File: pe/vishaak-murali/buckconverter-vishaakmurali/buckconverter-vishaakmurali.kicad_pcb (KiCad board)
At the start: 2 copper layers, 42 x 28 mm, 7 parts, among them J1 VIN_IN, J2 VOUT_5V, U1 AP63205WU

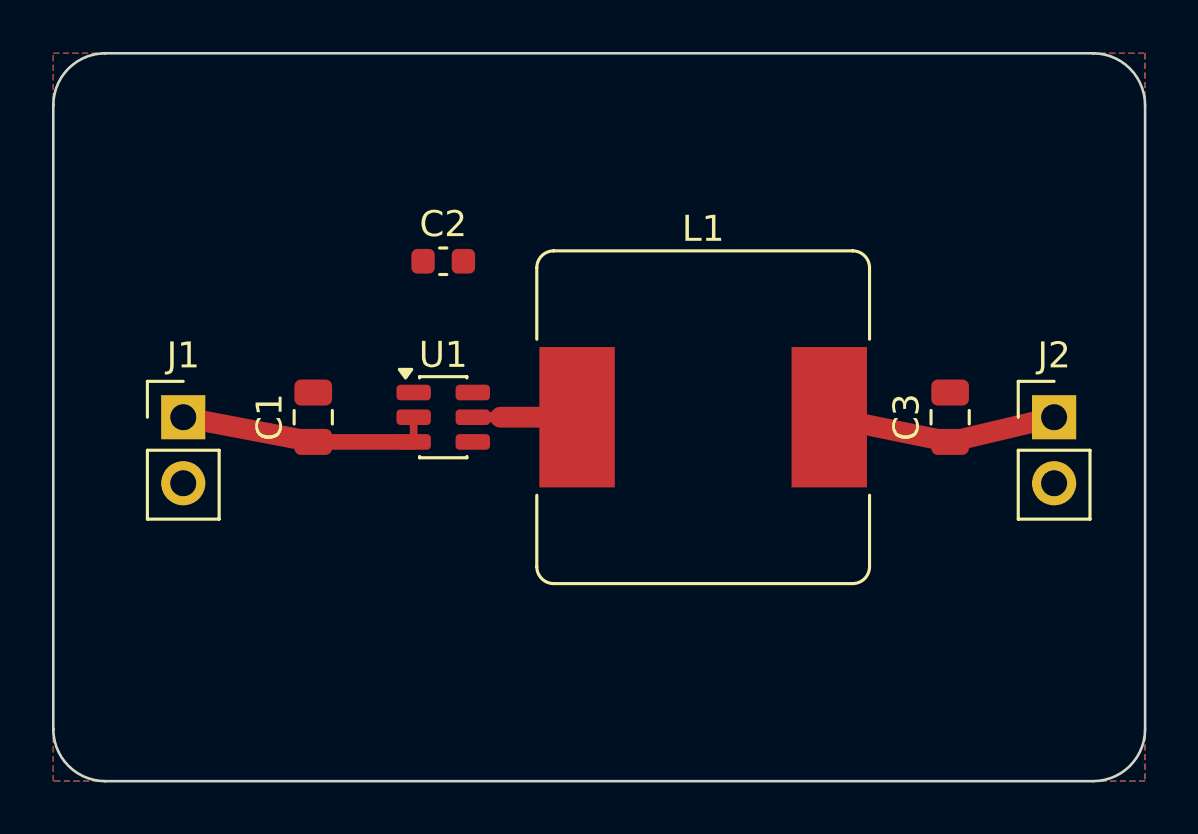
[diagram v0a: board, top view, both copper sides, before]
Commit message: fix buck schematic wiring and route pcb
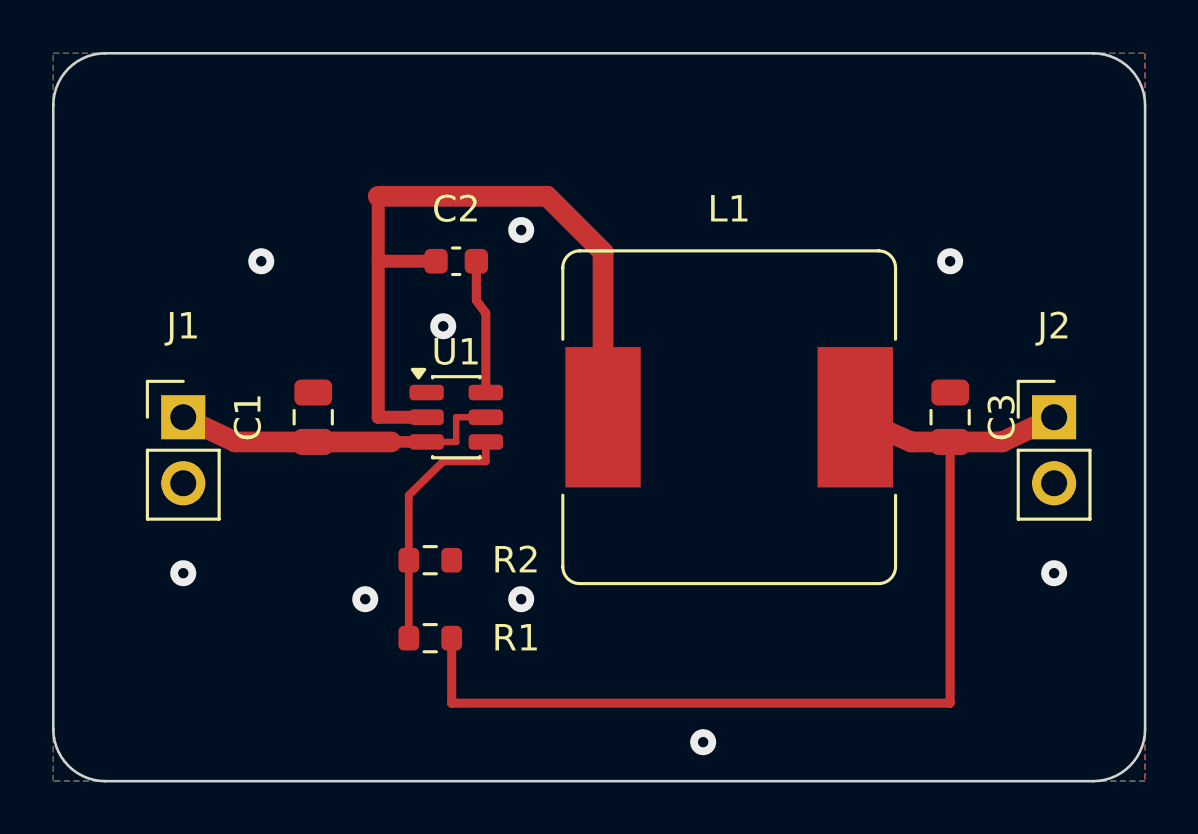
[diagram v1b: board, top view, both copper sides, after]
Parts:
- added R1: 100k, Resistor_SMD:R_0603_1608Metric, F.Cu at (114.5, 122.5)
- added R2: 13.3k, Resistor_SMD:R_0603_1608Metric, F.Cu at (114.5, 119.5)
- U1: value AP63205WU -> TPS54202DDC
- moved L1 1.00 mm to (126.0, 114.0)
- moved C2 0.50 mm to (115.5, 108.0), turned to 180 degrees
- moved U1 0.50 mm to (115.5, 114.0)
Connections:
- U1 pad 1: +5V -> GND
- U1 pad 2: VIN -> Net-(C2-Pad2)
- U1 pad 4: GND -> Net-(R1-Pad2)
- U1 pad 5: Net-(C2-Pad2) -> VIN
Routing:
- net +5V: track 8.86 -> 39.8 mm
- net Net-(C2-Pad2): track 4.01 -> 28.5 mm
- net Net-(R1-Pad2): track 0.00 -> 9.74 mm
- net Net-(C2-Pad1): track 0.00 -> 5.17 mm
- net VIN: track 9.90 -> 12.8 mm
- net GND: vias 0 -> 9
